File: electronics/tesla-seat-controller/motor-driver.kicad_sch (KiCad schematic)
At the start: 15 parts, among them J4 Motor A, J5 Motor B, U3 DRV8262DDWR

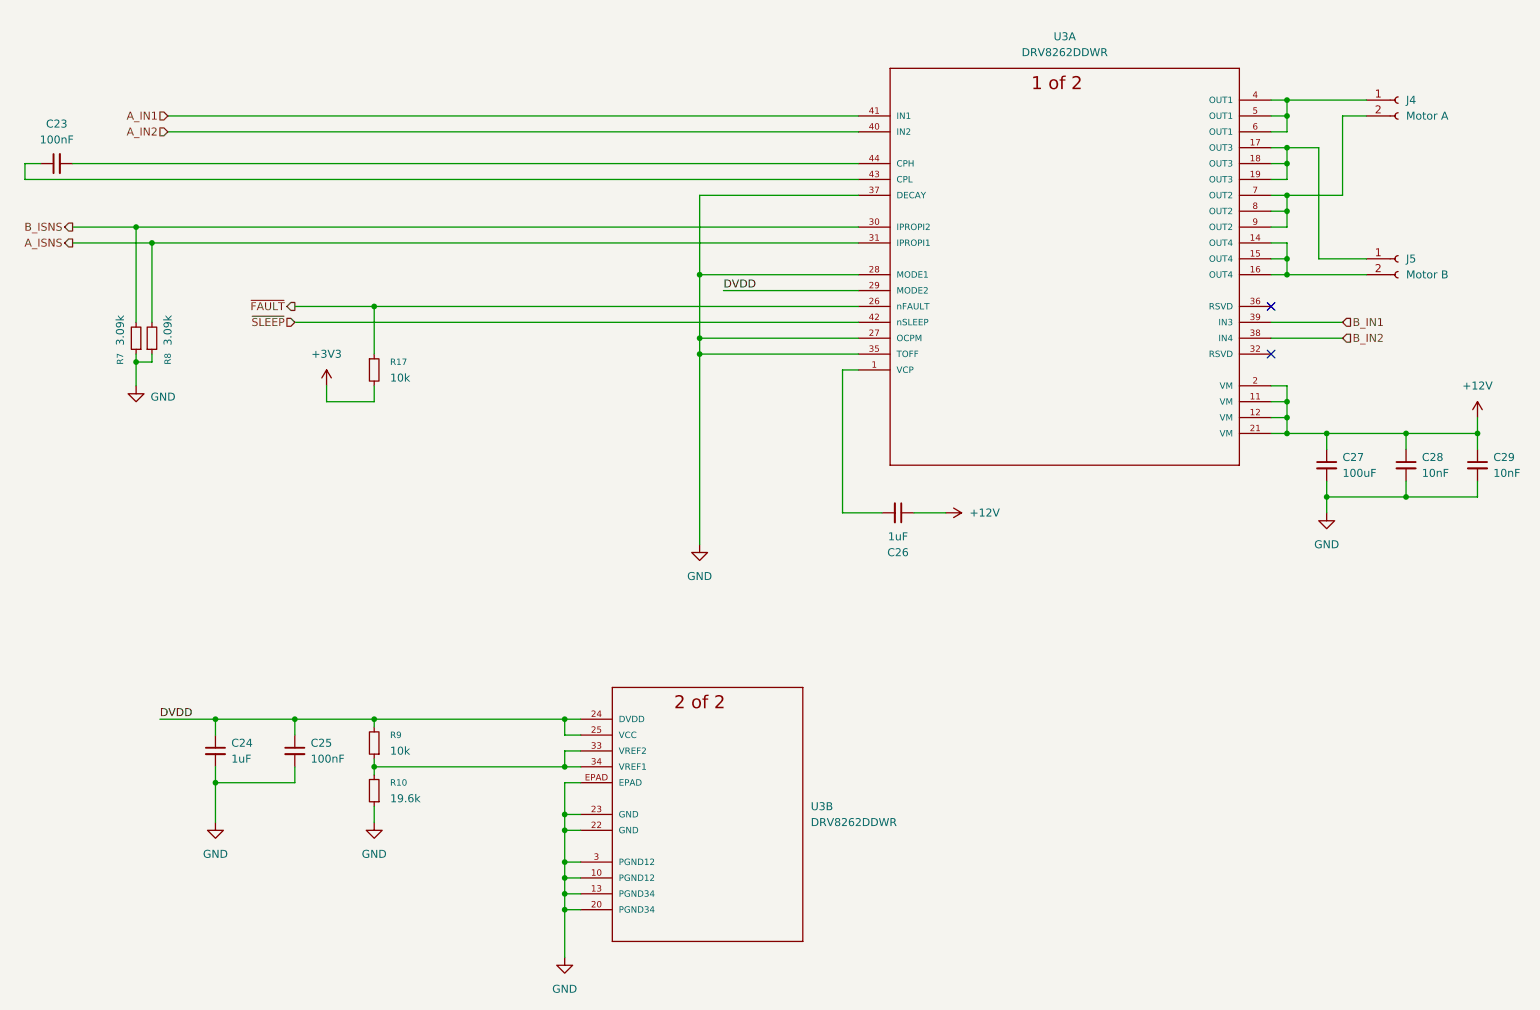
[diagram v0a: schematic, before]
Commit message: Audit fixes, DRV8262 DDV swap, 14.6A ITRIP, pin-contract tests
Schematic (all verified against datasheets, ERC clean):
- Flip D2 SMBJ16A TVS (was installed backwards, would short the 12V rail)
- C12 4.7nF -> 4.7uF (STM32 VDD bulk decoupling per DS13560)
- U2 now a proper Regulator_Switching:AP63203WU (symbol/value/lib_id were
  inconsistent AP63205WU with overridden value)
- D1 BZX84C15 -> BZX84C12 (Q1 IPD90P03P4L-04 VGS max is +5/-16V)
- Swap DRV8262DDWR -> DRV8262DDVR (top thermal pad for heatsink, 16A peak /
  10A RMS per output in dual H-bridge). Symbol pins renumbered in place per
  datasheet Table 4-1 so all wiring is untouched; EPAD pin/pad and its stub
  wires removed (DDV pad is heatsink-only). New HTSSOP44-DDV_TEX footprint
  derived from the DDW land pattern (44 pads, no thermal pad).
- ITRIP sized for max: R_IPROPI 3.09k -> 1.00k, VREF divider 19.6k -> 16.2k.
  ITRIP ~14.6A typ (13.3-16.0A tol band), deliberately under the DDV's 16A
  OCP minimum so current chopping always wins over latch-off. Also fixes
  VREF exceeding its 3.3V recommended max at DVDD tolerance extremes.
- F1: 7.5A slow-blow -> 10A mini blade fuse in Keystone 3568 holder
  (swappable rating for bring-up; motors' real stall current still unknown)

Tests:
- tests/pinmap.py: single-source-of-truth pin contract for the STM32G0B1
  (nets, timer/channel/AF claims, ADC channels, 5V-tolerance requirements)
- tests/test_pinmap.py: validates the contract against a fresh kicad-cli
  netlist export and DS13560 AF/ADC tables; catches moved pins, double-booked
  timer channels, CHx/CHxN complementary conflicts, split-timer motor pairs;
  self-test proves each checker can fail. Motor C is a documented TIM1+TIM14
  split (PA7 has no non-complementary TIM1 channel).

Cleanup: remove stray netlist/audit/report artifacts and lib backup;
ignore *.kicad_net.

Co-Authored-By: Claude Fable 5 <noreply@anthropic.com>
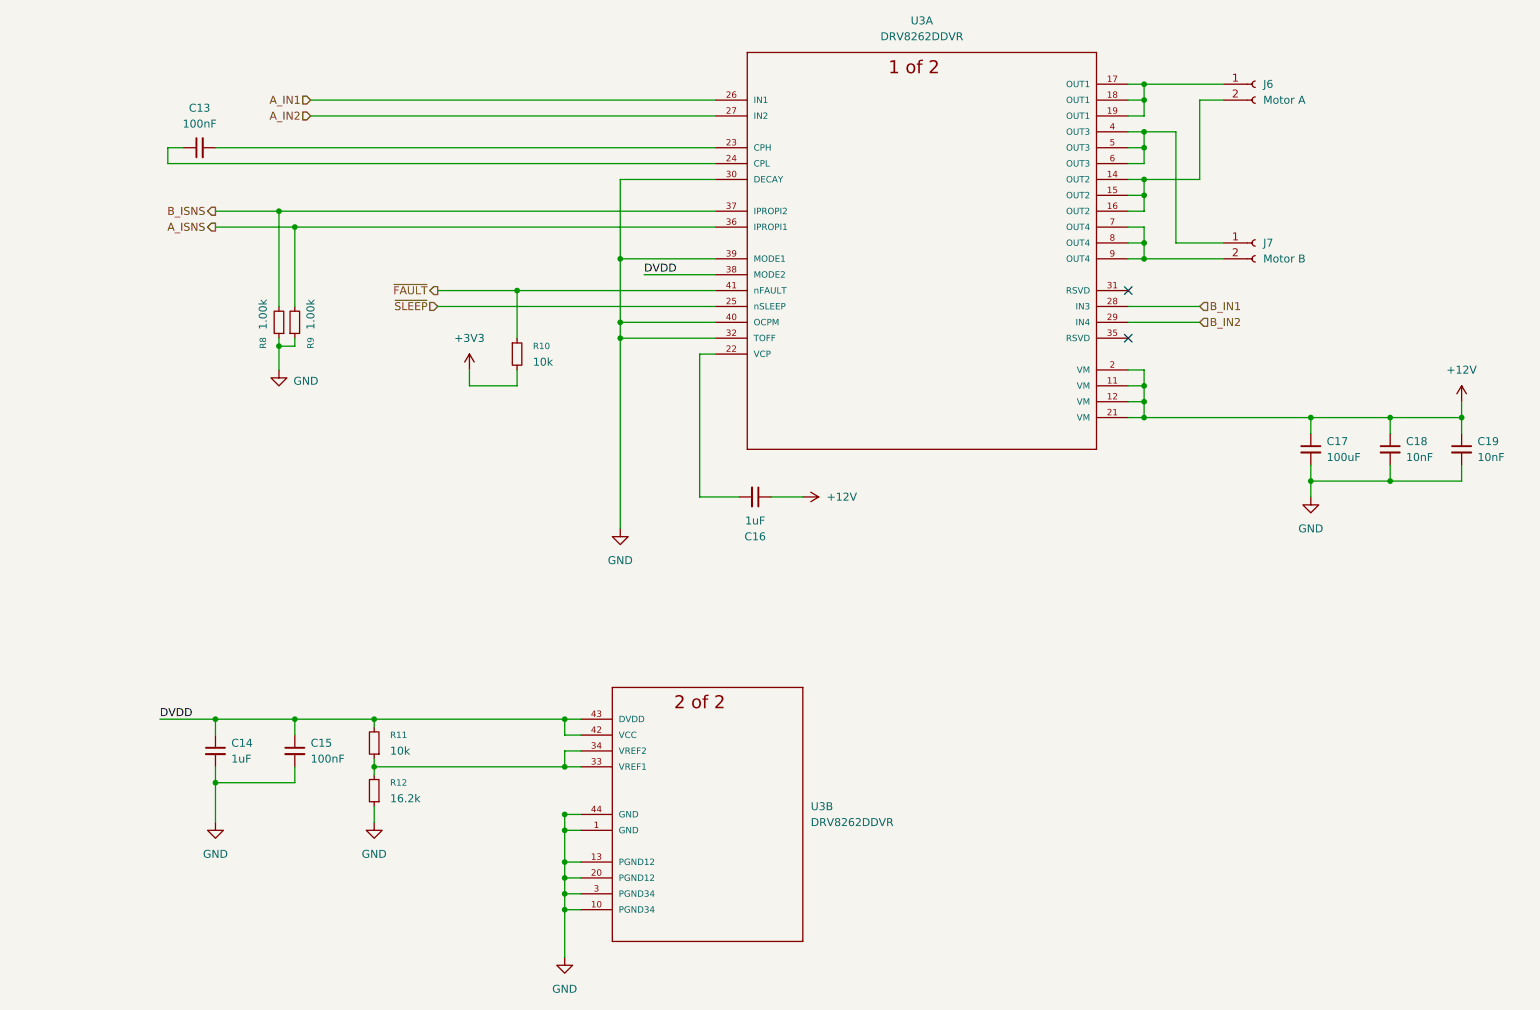
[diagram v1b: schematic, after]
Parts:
- R12: renamed from R10; value 19.6k -> 16.2k
- R8: renamed from R7; value 3.09k -> 1.00k
- R9: renamed from R8; value 3.09k -> 1.00k
- U3: value DRV8262DDWR -> DRV8262DDVR; footprint tesla-seat-controller:HTSSOP44-DDW_TEX -> tesla-seat-controller:HTSSOP44-DDV_TEX; symbol tesla-seat-controller:DRV8262DDWR -> tesla-seat-controller:DRV8262DDVR; Check_prices https://www.snapeda.com/parts/DRV8262DDWR/Texas+Instruments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 -> https://www.snapeda.com/parts/DRV8262DDVR/Texas+Instruments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; MANUFACTURER_PART_NUMBER DRV8262DDWR -> DRV8262DDVR; MP DRV8262DDWR -> DRV8262DDVR; SnapEDA_Link https://www.snapeda.com/parts/DRV8262DDWR/Texas+Instruments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 -> https://www.snapeda.com/parts/DRV8262DDVR/Texas+Instruments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
- renumbered C23 to C13, C24 to C14, C25 to C15, C26 to C16, C27 to C17, C28 to C18, C29 to C19, J4 to J6, J5 to J7, R17 to R10, R9 to R11
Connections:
- net A_IN1: now also U3.26 (IN1); no longer U3.41 (IN1)
- net A_IN2: now also U3.27 (IN2); no longer U3.40 (IN2)
- net A_ISNS: now also U3.36 (IPROPI1); no longer U3.31 (IPROPI1)
- net B_IN1: now also U3.28 (IN3); no longer U3.39 (IN3)
- net B_IN2: now also U3.29 (IN4); no longer U3.38 (IN4)
- net B_ISNS: now also U3.37 (IPROPI2); no longer U3.30 (IPROPI2)
- net DVDD: now also U3.38 (MODE2), U3.42 (VCC), U3.43 (DVDD); no longer U3.24 (DVDD), U3.25 (VCC), U3.29 (MODE2)
- net GND: now also U3.1 (GND), U3.30 (DECAY), U3.32 (TOFF), U3.39 (MODE1), U3.40 (OCPM), U3.44 (GND); no longer U3.22 (GND), U3.23 (GND), U3.27 (OCPM), U3.28 (MODE1), U3.35 (TOFF), U3.37 (DECAY), U3.EPAD
- net ~{FAULT}: now also U3.41 (nFAULT); no longer U3.26 (nFAULT)
- net ~{SLEEP}: now also U3.25 (nSLEEP); no longer U3.42 (nSLEEP)
- net at U3.17 (OUT1), U3.18 (OUT1), U3.19 (OUT1): now also J6.1 (Pin_1); no longer J7.1 (Pin_1)
- net at U3.14 (OUT2), U3.15 (OUT2), U3.16 (OUT2): now also J6.2 (Pin_2); no longer J7.2 (Pin_2)
- net at C16.2: now also U3.22 (VCP); no longer U3.1 (VCP)
- net at C13.1: now also U3.24 (CPL); no longer U3.43 (CPL)
- net at C13.2: now also U3.23 (CPH); no longer U3.44 (CPH)
- net at U3.4 (OUT3), U3.5 (OUT3), U3.6 (OUT3): now also J7.1 (Pin_1); no longer J6.1 (Pin_1)
- net at U3.7 (OUT4), U3.8 (OUT4), U3.9 (OUT4): now also J7.2 (Pin_2); no longer J6.2 (Pin_2)
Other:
- moved on the sheet: C13, C16, C17, C18, C19, J6, J7, R10, R8, R9, U3A

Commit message: Footprint/BOM pass: 0805 baseline for DIY reflow, side-exit connectors
- All passives 0805 (standard reflow pads, HandSolder variants normalized);
  exceptions: C3/C4/C5 in 1206 (10uF 50V, 22uF), C17/C24 upgraded
  100uF -> 220uF 35V polymer hybrid (CP_Elec 10x10.5) for the ~14.6A
  chopping level
- D1 BZX84C12 (SOT-23) -> BZT52C12 (SOD-123): same 12V zener, 2-pad
  package matches the 2-pin symbol and is easier to assemble
- D2 -> D_SMB, Q1 -> TO-252-2, L1 -> Bourns SRN6045TA (3.9uH, Isat ~5A)
- Connectors, all side-exit per harness preference: J1 XT30PW-M,
  J6-J9 XT30PW-F, J2/J3 JST S3B-XH-A, J5 JST S4B-XH-A
- README: BOM ordering notes (voltage ratings, MPNs, stencil spec)

Every component now has a footprint; ERC 0 violations; pinmap tests pass.

Co-Authored-By: Claude Fable 5 <noreply@anthropic.com>
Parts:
- C13, C14, C15, C16, C18, C19: footprint (none) -> Capacitor_SMD:C_0805_2012Metric
- C17: value 100uF -> 220uF 35V polymer; footprint (none) -> Capacitor_SMD:CP_Elec_10x10.5
- J6, J7: footprint (none) -> Connector_AMASS:AMASS_XT30PW-F_1x02_P2.50mm_Horizontal
- R10, R11, R12, R8, R9: footprint (none) -> Resistor_SMD:R_0805_2012Metric
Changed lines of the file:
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@@
 			)
 		)
-		(property "Footprint" ""
+		(property "Footprint" "Connector_AMASS:AMASS_XT30PW-F_1x02_P2.50mm_Horizontal"
 			(at 217.17 63.5 0)
 			(hide yes)
@@
 			)
 		)
-		(property "Footprint" ""
+		(property "Footprint" "Capacitor_SMD:C_0805_2012Metric"
 			(at 137.16 104.14 0)
 			(hide yes)
@@
 			)
 		)
-		(property "Footprint" ""
+		(property "Footprint" "Capacitor_SMD:C_0805_2012Metric"
 			(at 48.26 48.26 0)
 			(hide yes)
@@
 			)
 		)
-		(property "Footprint" ""
+		(property "Footprint" "Resistor_SMD:R_0805_2012Metric"
 			(at 76.2 143.51 0)
 			(hide yes)
@@
 			)
 		)
-		(property "Footprint" ""
+		(property "Footprint" "Connector_AMASS:AMASS_XT30PW-F_1x02_P2.50mm_Horizontal"
 			(at 217.17 38.1 0)
 			(hide yes)
@@
 			)
 		)
-		(property "Footprint" ""
+		(property "Footprint" "Capacitor_SMD:C_0805_2012Metric"
 			(at 238.76 96.52 0)
 			(hide yes)
@@
 			)
 		)
-		(property "Footprint" ""
+		(property "Footprint" "Resistor_SMD:R_0805_2012Metric"
 			(at 60.96 76.2 0)
 			(hide yes)
@@
 			)
 		)
-		(property "Footprint" ""
+		(property "Footprint" "Capacitor_SMD:C_0805_2012Metric"
 			(at 250.19 96.52 0)
 			(hide yes)
@@
 			)
 		)
-		(property "Footprint" ""
+		(property "Footprint" "Capacitor_SMD:C_0805_2012Metric"
 			(at 50.8 144.78 0)
 			(hide yes)
@@
 			)
 		)
-		(property "Footprint" ""
+		(property "Footprint" "Resistor_SMD:R_0805_2012Metric"
 			(at 76.2 151.13 0)
 			(hide yes)
@@
 			)
 		)
-		(property "Value" "100uF"
+		(property "Value" "220uF 35V polymer"
 			(at 228.6 97.7962 0)
 			(show_name no)
@@
 			)
 		)
-		(property "Footprint" ""
+		(property "Footprint" "Capacitor_SMD:CP_Elec_10x10.5"
 			(at 226.06 96.52 0)
 			(hide yes)
@@
 			)
 		)
-		(property "Footprint" ""
+		(property "Footprint" "Capacitor_SMD:C_0805_2012Metric"
 			(at 63.5 144.78 0)
 			(hide yes)
@@
 			)
 		)
-		(property "Footprint" ""
+		(property "Footprint" "Resistor_SMD:R_0805_2012Metric"
 			(at 63.5 76.2 0)
 			(hide yes)
@@
 			)
 		)
-		(property "Footprint" ""
+		(property "Footprint" "Resistor_SMD:R_0805_2012Metric"
 			(at 99.06 81.28 0)
 			(hide yes)

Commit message: Add schematic title blocks
Co-Authored-By: Claude Fable 5 <noreply@anthropic.com>
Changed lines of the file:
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@@
 	(generator_version "10.0")
 	(paper "A4")
+	(title_block
+		(date "2026-07-17")
+	)
 	(junction
 		(at 76.2 139.7)
@@
 		(diameter 0)
 		(color 0 0 0 0)
-	)
-	(junction
-		(at 106.68 154.94)
-		(diameter 0)
-		(color 0 0 0 0)
